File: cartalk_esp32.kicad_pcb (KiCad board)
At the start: 2 copper layers, 25 parts, among them IC1 CP2104, J1 10118192-0002LF, Q1 mmbt2222, Q2 mmbt2222, SW2 KMR2, U1 HUB75 Connector Female, U2 AP2112-3.3, X2 ESP32_WROOM32_SKINNY, X4 20329

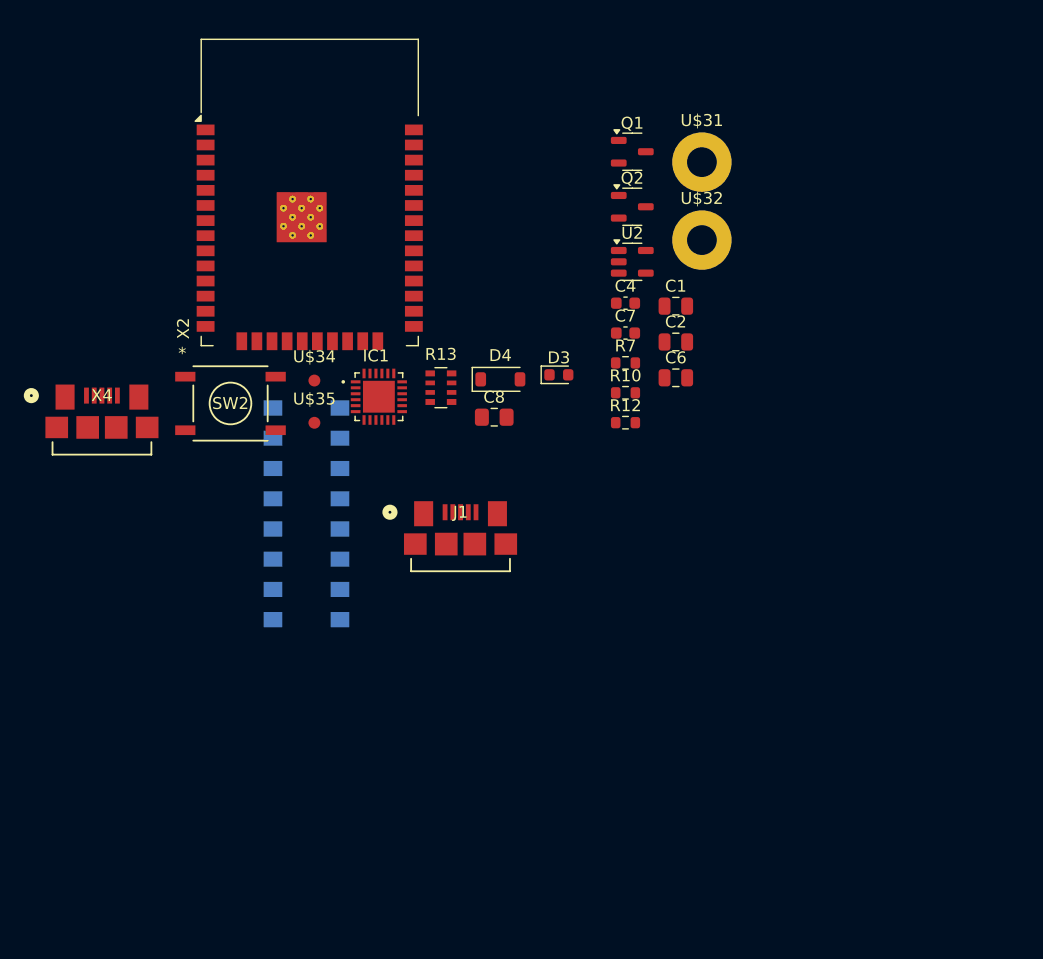
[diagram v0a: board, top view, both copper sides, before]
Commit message: Fix remaining symbol-footprint pin mismatches.
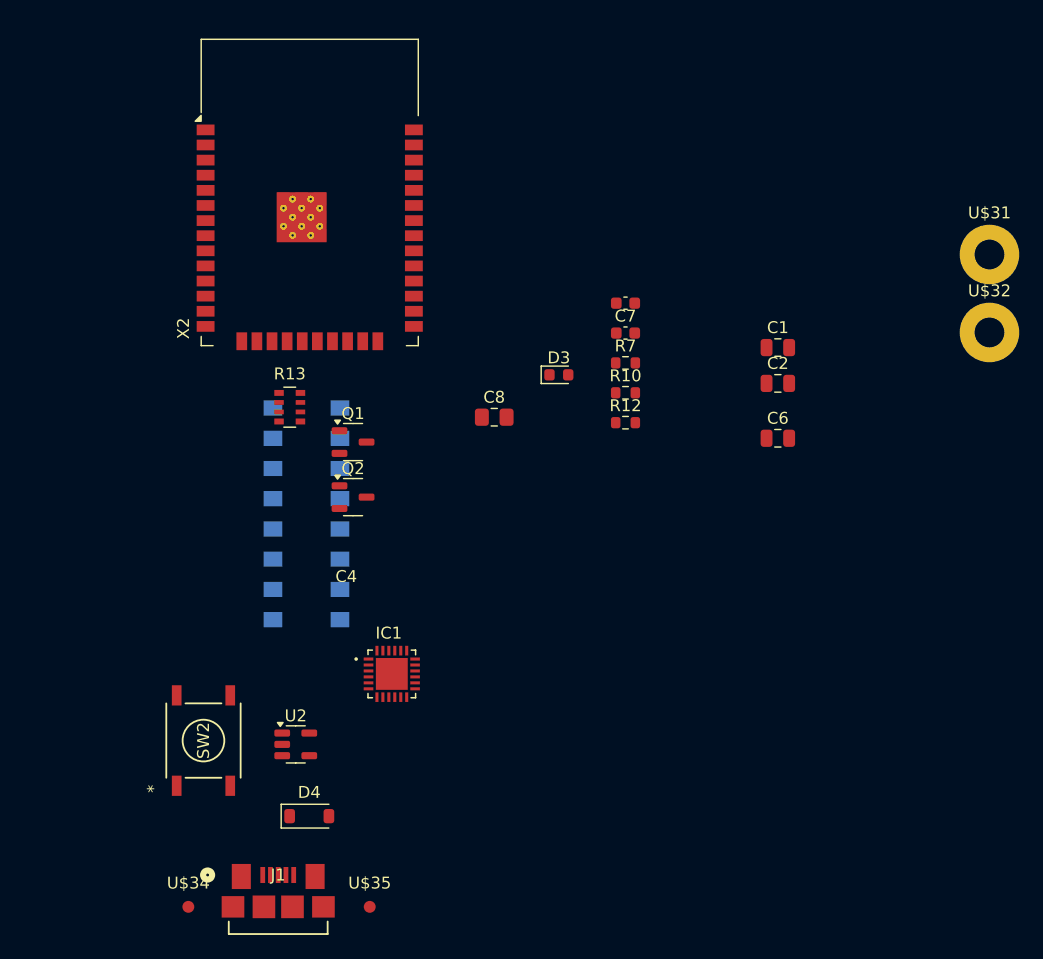
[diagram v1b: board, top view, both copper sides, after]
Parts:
- removed X4: 20329, smd_usb_micro_b_connector:CONN_10118192-0002LF_AMP
- moved U2 49.4 mm to (128.4, 141.3)
- moved U$34 45.5 mm to (119.4, 154.9)
- moved U$35 40.9 mm to (134.6, 154.9)
- moved D4 40.1 mm to (129.5, 147.3)
- moved J1 34.1 mm to (126.9, 154.5)
- moved Q1 33.8 mm to (133.2, 115.9)
- moved Q2 33.8 mm to (133.2, 120.5)
- moved SW2 28.4 mm to (120.7, 141.0), turned to 90 degrees
- moved U$32 25.4 mm to (186.7, 106.7)
- moved U$31 25.4 mm to (186.7, 100.1)
- moved IC1 23.3 mm to (136.5, 135.4)
- moved R13 12.8 mm to (127.9, 113.0)
- moved C6 9.96 mm to (168.9, 115.6)
- moved C1 9.25 mm to (168.9, 108.0)
- moved C2 9.25 mm to (168.9, 111.0)
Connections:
- C6 pad 1: Net-(U2-IN) -> Net-(D4-C)
- D3 pad 1: (no net) -> Net-(D3-A)
- D3 pad 2: (no net) -> GND
- D4 pad 1: (no net) -> VBUS
- D4 pad 2: (no net) -> Net-(D4-C)
- IC1 pad 25: (no net) -> GND
- R10 pad 2: Net-(D3-PadA) -> Net-(D3-A)
- R7 pad 2: Net-(U2-IN) -> Net-(D4-C)
- SW2 pad 1: (no net) -> GND
- SW2 pad 2: (no net) -> GND
- SW2 pad 3: (no net) -> /RESET
- SW2 pad 4: (no net) -> /RESET
- U1 pad 2: <NO NET> -> GND
- U1 pad 4: <NO NET> -> GND
- U1 pad 8: <NO NET> -> GND
- U2 pad 1: Net-(U2-IN) -> Net-(D4-C)
- X2 pad 38: GND -> unconnected-(X2-NC-Pad38)
- X2 pad 39: unconnected-(X2-BASE_GND-Pad39) -> GND

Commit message: Organize the pcb layout some.
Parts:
- moved U1 26.7 mm to (130.5, 95.2)
- moved C8 24.3 mm to (167.9, 105.4)
- moved R7 20.3 mm to (155.4, 129.5)
- moved C4 16.1 mm to (143.5, 114.3)
- moved R10 13.0 mm to (145.6, 119.4)
- moved Q2 12.5 mm to (123.3, 112.9), turned to 180 degrees
- moved C7 12.3 mm to (168.1, 109.2)
- moved C6 6.48 mm to (167.6, 121.9)
- moved IC1 5.76 mm to (135.2, 141.0)
- moved R12 5.76 mm to (158.8, 119.4)
- moved C1 3.81 mm to (168.9, 111.8)
- moved C2 3.34 mm to (168.9, 114.3)
- moved Q1 3.03 mm to (132.2, 113.0)
- turned D3 to 180 degrees

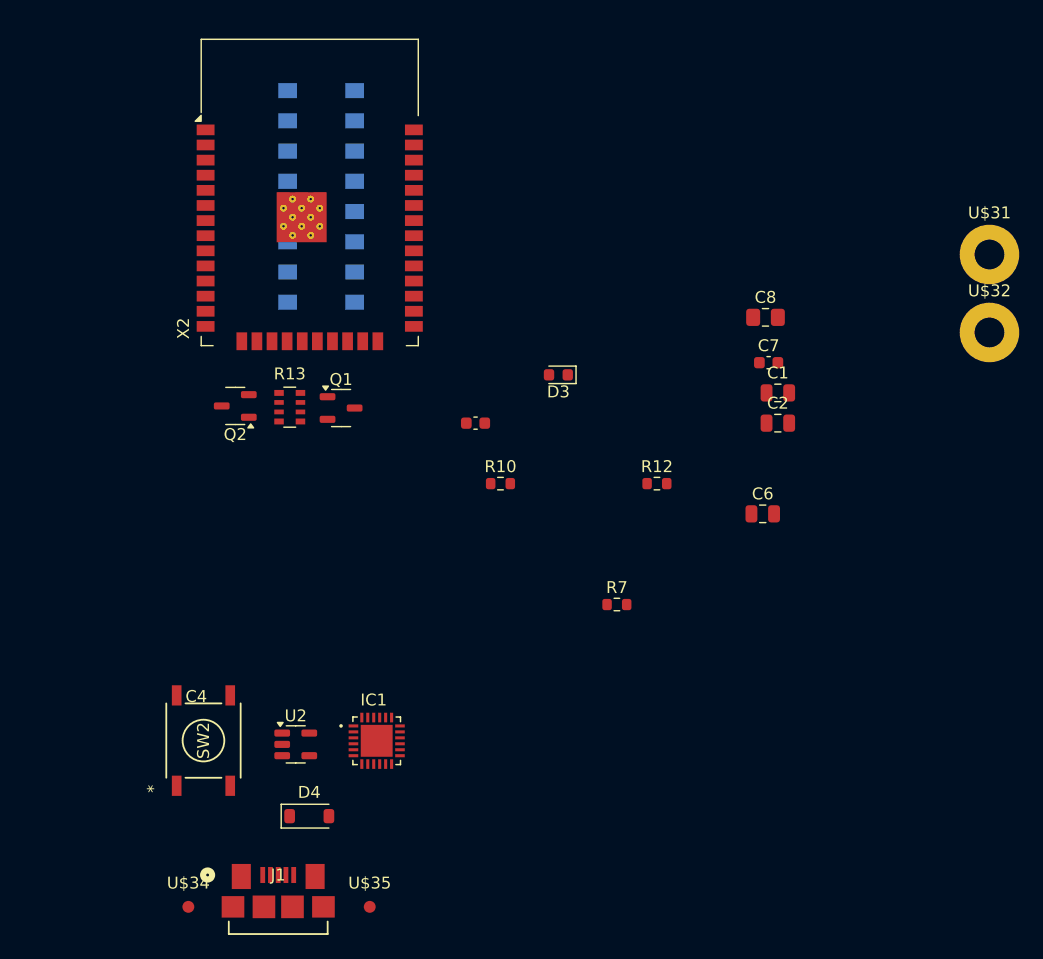
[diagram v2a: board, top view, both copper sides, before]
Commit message: Update component layout on board to fit in a small amount of space.
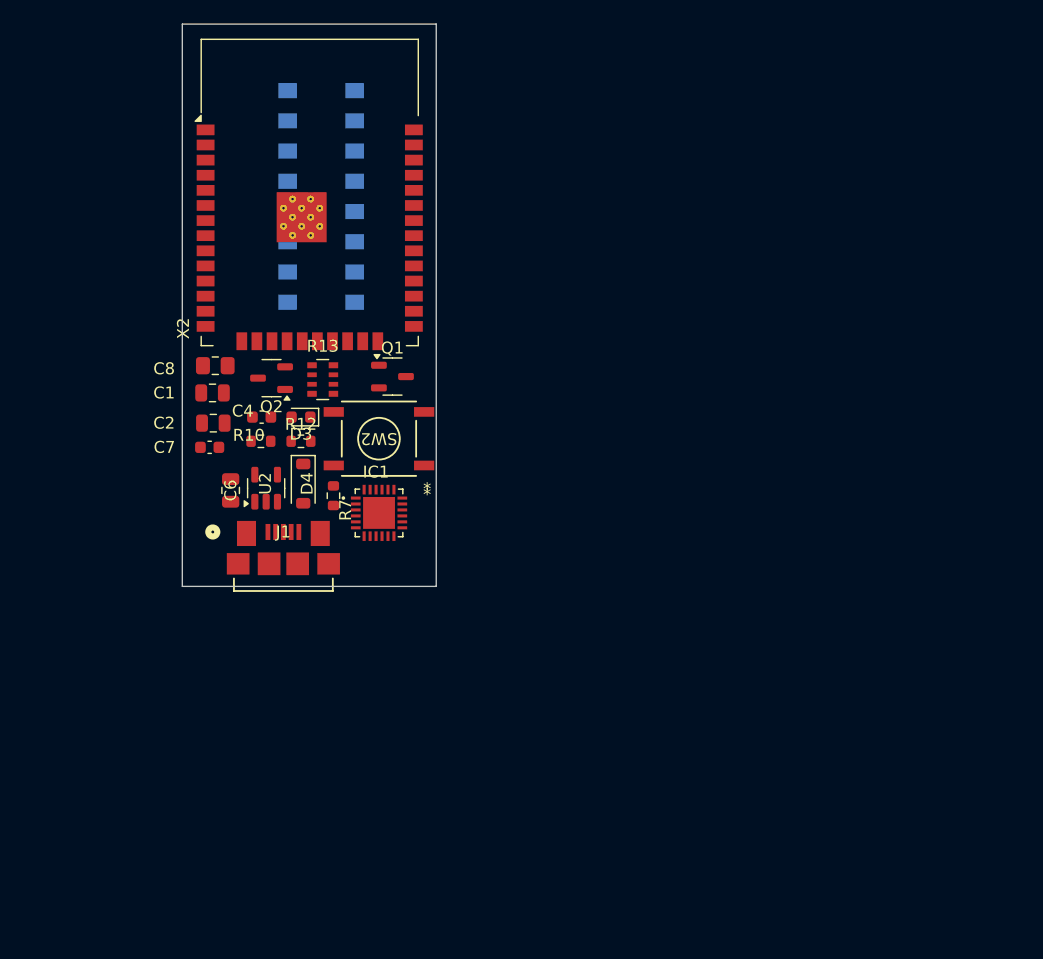
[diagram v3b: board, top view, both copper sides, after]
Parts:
- removed U$31, U$32: MOUNTINGHOLE2.5, MountingHole:MountingHole_2.5mm_Pad
- removed U$34, U$35: FIDUCIAL_1MM, Fiducial:Fiducial_1mm_Mask2mm
- moved C7 47.5 mm to (121.2, 116.3)
- moved C1 47.5 mm to (121.4, 111.8)
- moved C2 47.4 mm to (121.5, 114.3)
- moved C8 46.4 mm to (121.6, 109.5)
- moved C6 44.7 mm to (122.9, 120.0), turned to 90 degrees
- moved R12 30.1 mm to (128.8, 115.8)
- moved SW2 29.3 mm to (135.4, 115.6), turned to 180 degrees
- moved J1 28.8 mm to (127.4, 125.6)
- moved D4 27.9 mm to (129.0, 119.4), turned to -90 degrees
- moved R7 25.5 mm to (131.6, 120.4), turned to -90 degrees
- moved D3 21.9 mm to (128.8, 113.8)
- moved U2 21.7 mm to (125.9, 119.8), turned to 90 degrees
- moved R10 20.4 mm to (125.5, 115.8)
- moved IC1 19.1 mm to (135.4, 121.8)
- moved C4 18.0 mm to (125.5, 113.8)
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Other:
- board outline added: 21.3 x 47.2 mm

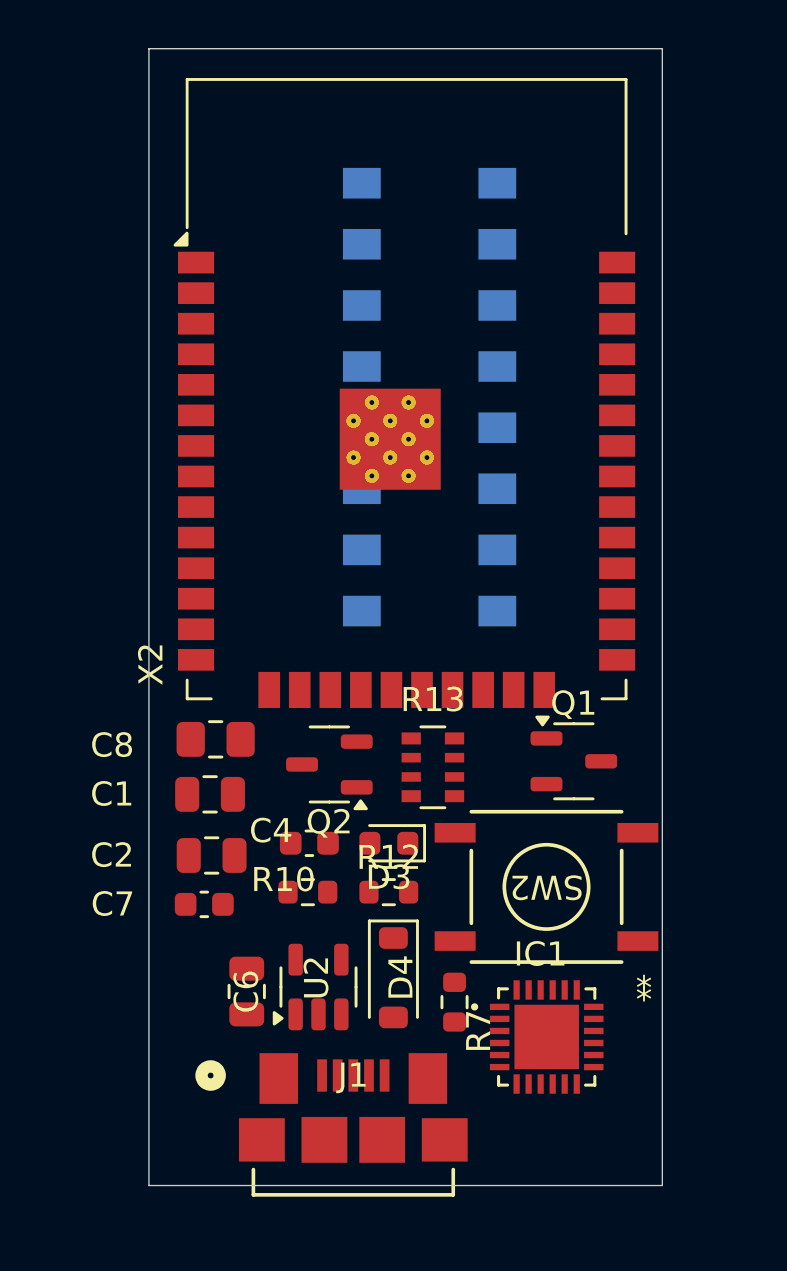
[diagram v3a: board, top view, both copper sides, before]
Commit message: Add power pads for soldering on 5V.
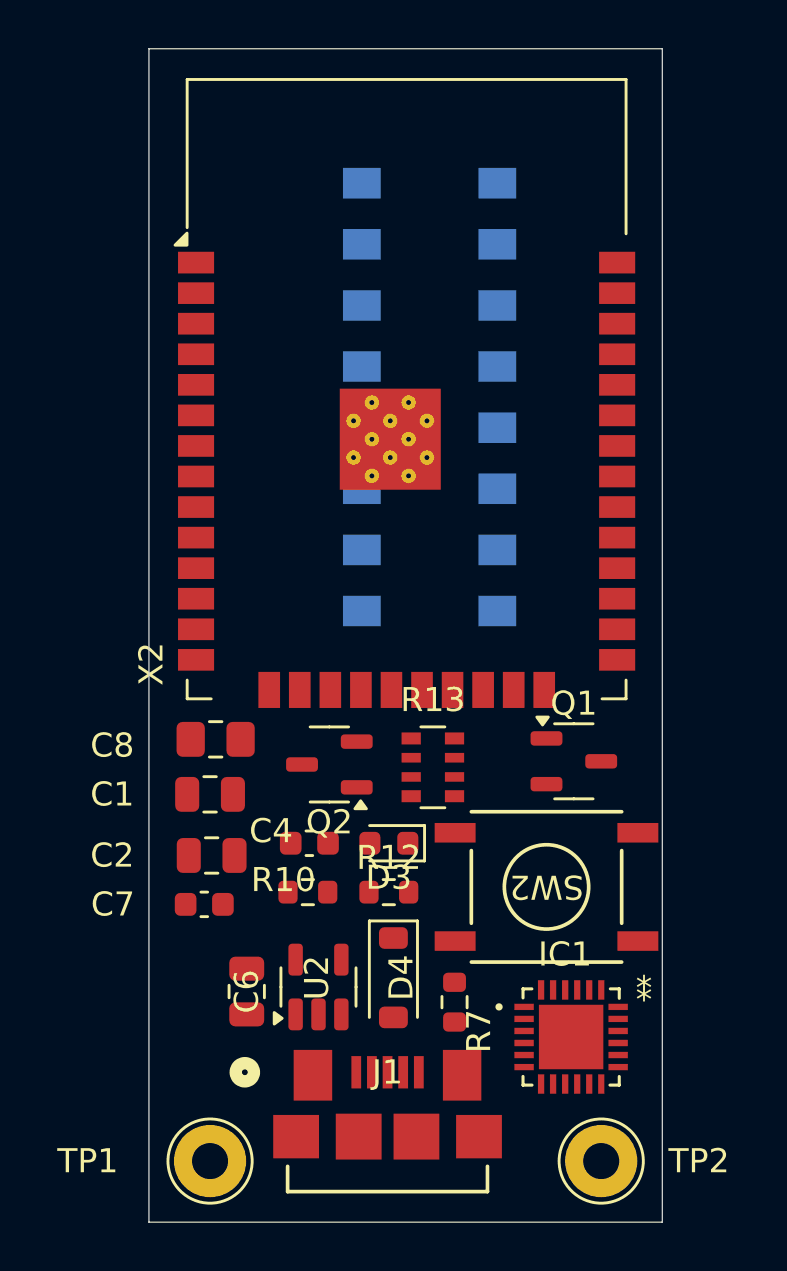
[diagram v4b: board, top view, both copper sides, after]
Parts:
- added TP1: TestPoint, TestPoint:TestPoint_THTPad_D3.0mm_Drill1.5mm, F.Cu at (121.4, 127.0)
- added TP2: TestPoint, TestPoint:TestPoint_THTPad_D3.0mm_Drill1.5mm, F.Cu at (137.7, 127.0)
- moved J1 1.43 mm to (128.8, 125.5)
- moved IC1 1.02 mm to (136.4, 121.8)
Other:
- board size 21.3 x 47.2 mm -> 21.3 x 48.8 mm
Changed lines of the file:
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@@
 		)
 	)
+	(footprint "TestPoint:TestPoint_THTPad_D3.0mm_Drill1.5mm"
+		(layer "F.Cu")
+		(at 137.668 127)
+		(descr "THT pad as test Point, diameter 3.0mm, hole diameter 1.5mm")
+		(tags "test point THT pad")
+		(property "Reference" "TP2"
+			(at 4.064 0 0)
+			(layer "F.SilkS")
+			(effects
+				(font
+					(size 1 1)
+					(thickness 0.15)
+				)
+			)
+		)
+		(property "Value" "TestPoint"
+			(at 0 2.55 0)
+			(layer "F.Fab")
+			(effects
+				(font
+					(size 1 1)
+					(thickness 0.15)
+				)
+			)
+		)
+		(property "Footprint" "TestPoint:TestPoint_THTPad_D3.0mm_Drill1.5mm"
+			(at 0 0 0)
+			(unlocked yes)
+			(layer "F.Fab")
+			(hide yes)
+			(effects
+				(font
+					(size 1.27 1.27)
+				)
+			)
+		)
+		(property "Datasheet" ""
+			(at 0 0 0)
+			(unlocked yes)
+			(layer "F.Fab")
+			(hide yes)
+			(effects
+				(font
+					(size 1.27 1.27)
+				)
+			)
+		)
+		(property "Description" "test point"
+			(at 0 0 0)
+			(unlocked yes)
+			(layer "F.Fab")
+			(hide yes)
+			(effects
+				(font
+					(size 1.27 1.27)
+				)
+			)
+		)
+		(property ki_fp_filters "Pin* Test*")
+		(sheetname "Root")
+		(sheetfile "cartalk_esp32.kicad_sch")
+		(attr exclude_from_pos_files)
+		(fp_circle
+			(center 0 0)
+			(end 0 1.75)
+			(stroke
+				(width 0.12)
+				(type solid)
+			)
+			(fill none)
+			(layer "F.SilkS")
+		)
+		(fp_circle
+			(center 0 0)
+			(end 2 0)
+			(stroke
+				(width 0.05)
+				(type solid)
+			)
+			(fill none)
+			(layer "F.CrtYd")
+		)
+		(fp_text user "${REFERENCE}"
+			(at 0 -2.4 0)
+			(layer "F.Fab")
+			(effects
+				(font
+					(size 1 1)
+					(thickness 0.15)
+				)
+			)
+		)
+		(pad "1" thru_hole circle
+			(at 0 0)
+			(size 3 3)
+			(drill 1.5)
+			(layers "*.Cu" "*.Mask")
+			(remove_unused_layers no)
+			(net 1 "GND")
+			(pinfunction "1")
+			(pintype "passive")
+		)
+	)
 	(footprint "Capacitor_SMD:C_0805_2012Metric"
 		(layer "F.Cu")
@@
 	(footprint "CP2104:QFN50P400X400X80-25N"
 		(layer "F.Cu")
-		(at 135.402 121.843)
+		(at 136.418 121.843)
 		(property "Reference" "IC1"
 			(at -0.25427 -3.43257 0)
@@
 	(footprint "smd_usb_micro_b_connector:CONN_10118192-0002LF_AMP"
 		(layer "F.Cu")
-		(at 127.366001 125.6479)
+		(at 128.788 125.512899)
 		(tags "10118192-0002LF ")
 		(property "Reference" "J1"
@@
 		)
 	)
+	(footprint "TestPoint:TestPoint_THTPad_D3.0mm_Drill1.5mm"
+		(layer "F.Cu")
+		(at 121.412 127)
+		(descr "THT pad as test Point, diameter 3.0mm, hole diameter 1.5mm")
+		(tags "test point THT pad")
+		(property "Reference" "TP1"
+			(at -5.08 0 0)
+			(layer "F.SilkS")
+			(effects
+				(font
+					(size 1 1)
+					(thickness 0.15)
+				)
+			)
+		)
+		(property "Value" "TestPoint"
+			(at 0 2.55 0)
+			(layer "F.Fab")
+			(effects
+				(font
+					(size 1 1)
+					(thickness 0.15)
+				)
+			)
+		)
+		(property "Footprint" "TestPoint:TestPoint_THTPad_D3.0mm_Drill1.5mm"
+			(at 0 0 0)
+			(unlocked yes)
+			(layer "F.Fab")
+			(hide yes)
+			(effects
+				(font
+					(size 1.27 1.27)
+				)
+			)
+		)
+		(property "Datasheet" ""
+			(at 0 0 0)
+			(unlocked yes)
+			(layer "F.Fab")
+			(hide yes)
+			(effects
+				(font
+					(size 1.27 1.27)
+				)
+			)
+		)
+		(property "Description" "test point"
+			(at 0 0 0)
+			(unlocked yes)
+			(layer "F.Fab")
+			(hide yes)
+			(effects
+				(font
+					(size 1.27 1.27)
+				)
+			)
+		)
+		(property ki_fp_filters "Pin* Test*")
+		(sheetname "Root")
+		(sheetfile "cartalk_esp32.kicad_sch")
+		(attr exclude_from_pos_files)
+		(fp_circle
+			(center 0 0)
+			(end 0 1.75)
+			(stroke
+				(width 0.12)
+				(type solid)
+			)
+			(fill none)
+			(layer "F.SilkS")
+		)
+		(fp_circle
+			(center 0 0)
+			(end 2 0)
+			(stroke
+				(width 0.05)
+				(type solid)
+			)
+			(fill none)
+			(layer "F.CrtYd")
+		)
+		(fp_text user "${REFERENCE}"
+			(at 0 -2.4 0)
+			(layer "F.Fab")
+			(effects
+				(font
+					(size 1 1)
+					(thickness 0.15)
+				)
+			)
+		)
+		(pad "1" thru_hole circle
+			(at 0 0)
+			(size 3 3)
+			(drill 1.5)
+			(layers "*.Cu" "*.Mask")
+			(remove_unused_layers no)
+			(net 12 "VBUS")
+			(pinfunction "1")
+			(pintype "passive")
+		)
+	)
 	(footprint "Connector:Amphenol 2x8 Connector 89898-308ALF"
 		(layer "B.Cu")
@@
 	(gr_rect
 		(start 118.872 80.772)
-		(end 140.208 128.016)
+		(end 140.208 129.54)
 		(stroke
 			(width 0.05)
